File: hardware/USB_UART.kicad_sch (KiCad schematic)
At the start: 5 parts, among them U13 CP2102N-QFN20

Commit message: working on io fugtions
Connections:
- net GND: now also U13.12 (GND), U13.21 (GND), U13.3 (GND)
- no-connect marks 0 -> 4
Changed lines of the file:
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@@
   (junction (at 153.67 41.91) (diameter 0) (color 0 0 0 0)
   )
+  (no_connect (at 194.31 87.63))
+  (no_connect (at 194.31 82.55))
+  (no_connect (at 194.31 80.01))
+  (no_connect (at 194.31 85.09))
   (wire (pts (xy 165.1 62.23) (xy 168.91 62.23))
     (stroke (width 0) (type default))
@@
   )
   (wire (pts (xy 171.45 30.48) (xy 180.34 30.48))
+    (stroke (width 0) (type default))
+  )
+  (wire (pts (xy 181.61 100.33) (xy 181.61 102.87))
     (stroke (width 0) (type default))
   )
@@
         )
       )
+    )
+  )
+  (symbol (lib_name "GND_1") (lib_id "power:GND") (at 181.61 102.87 0) (unit 1)
+    (in_bom yes) (on_board yes) (dnp no) (fields_autoplaced)
+    (property "Reference" "#PWR076" (at 181.61 109.22 0)
+      (effects (font (size 1.27 1.27)) hide)
+    )
+    (property "Value" "GND" (at 181.61 107.95 0)
+      (effects (font (size 1.27 1.27)))
+    )
+    (property "Footprint" "" (at 181.61 102.87 0)
+      (effects (font (size 1.27 1.27)) hide)
+    )
+    (property "Datasheet" "" (at 181.61 102.87 0)
+      (effects (font (size 1.27 1.27)) hide)
+    )
+    (pin "1")
+    (instances
+      (project "usbc-car-module"
+        (path "/fae025e9-99c5-40c1-af6f-99dc1edbfa43/115036d9-3633-4f5d-a259-54a6f0cf58ce"
+          (reference "#PWR076") (unit 1)
+        )
+      )

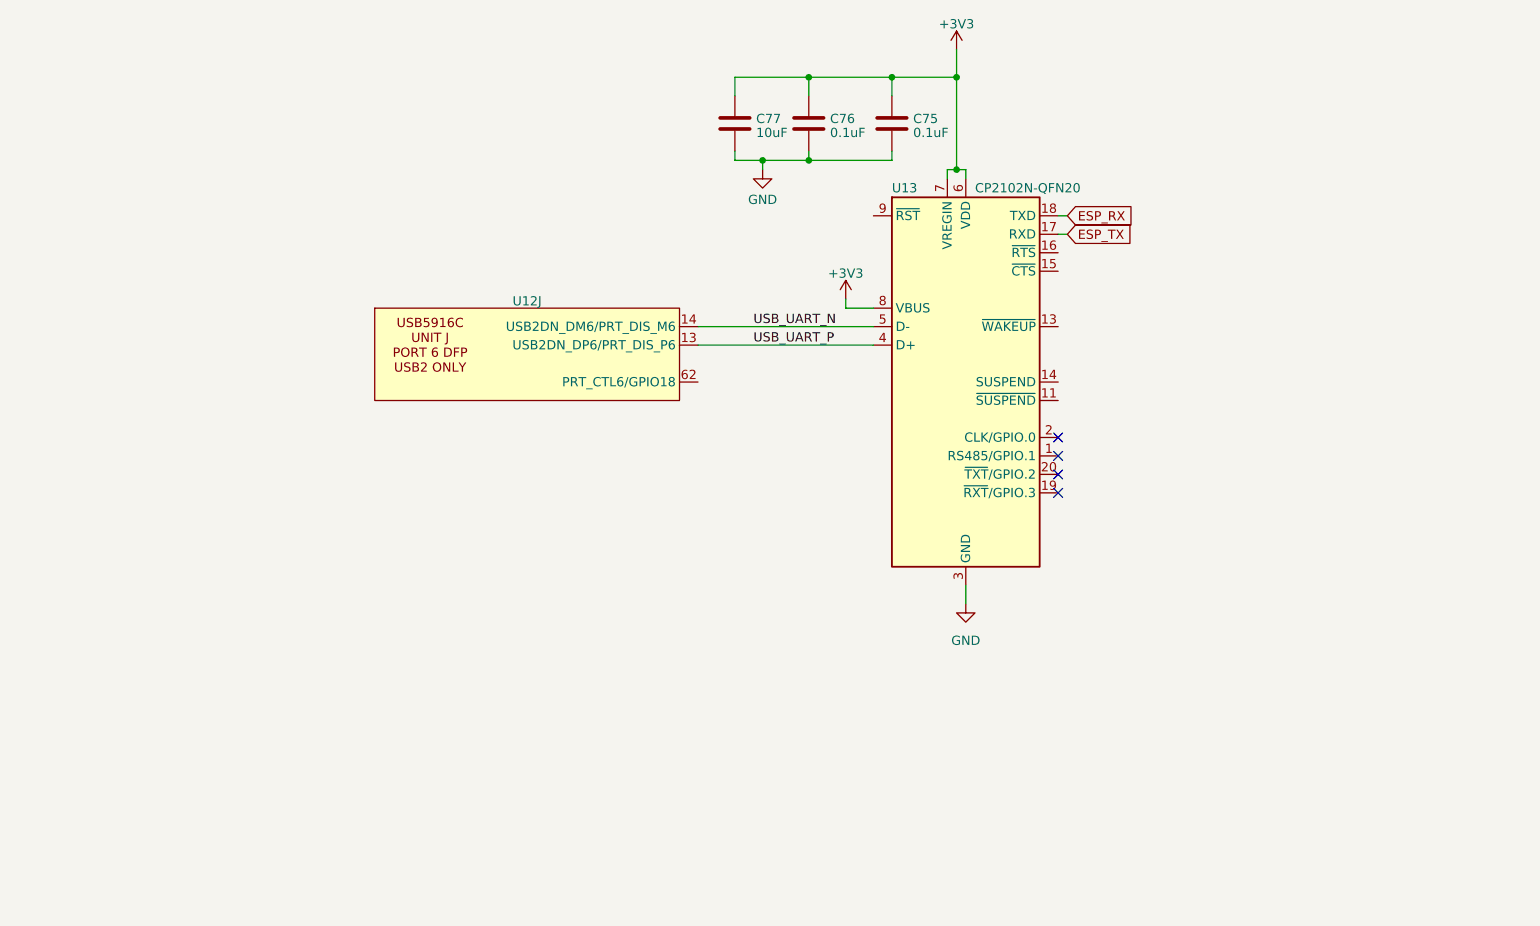
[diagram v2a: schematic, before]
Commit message: working on hardware agin as well as implimentded auto adc init and read
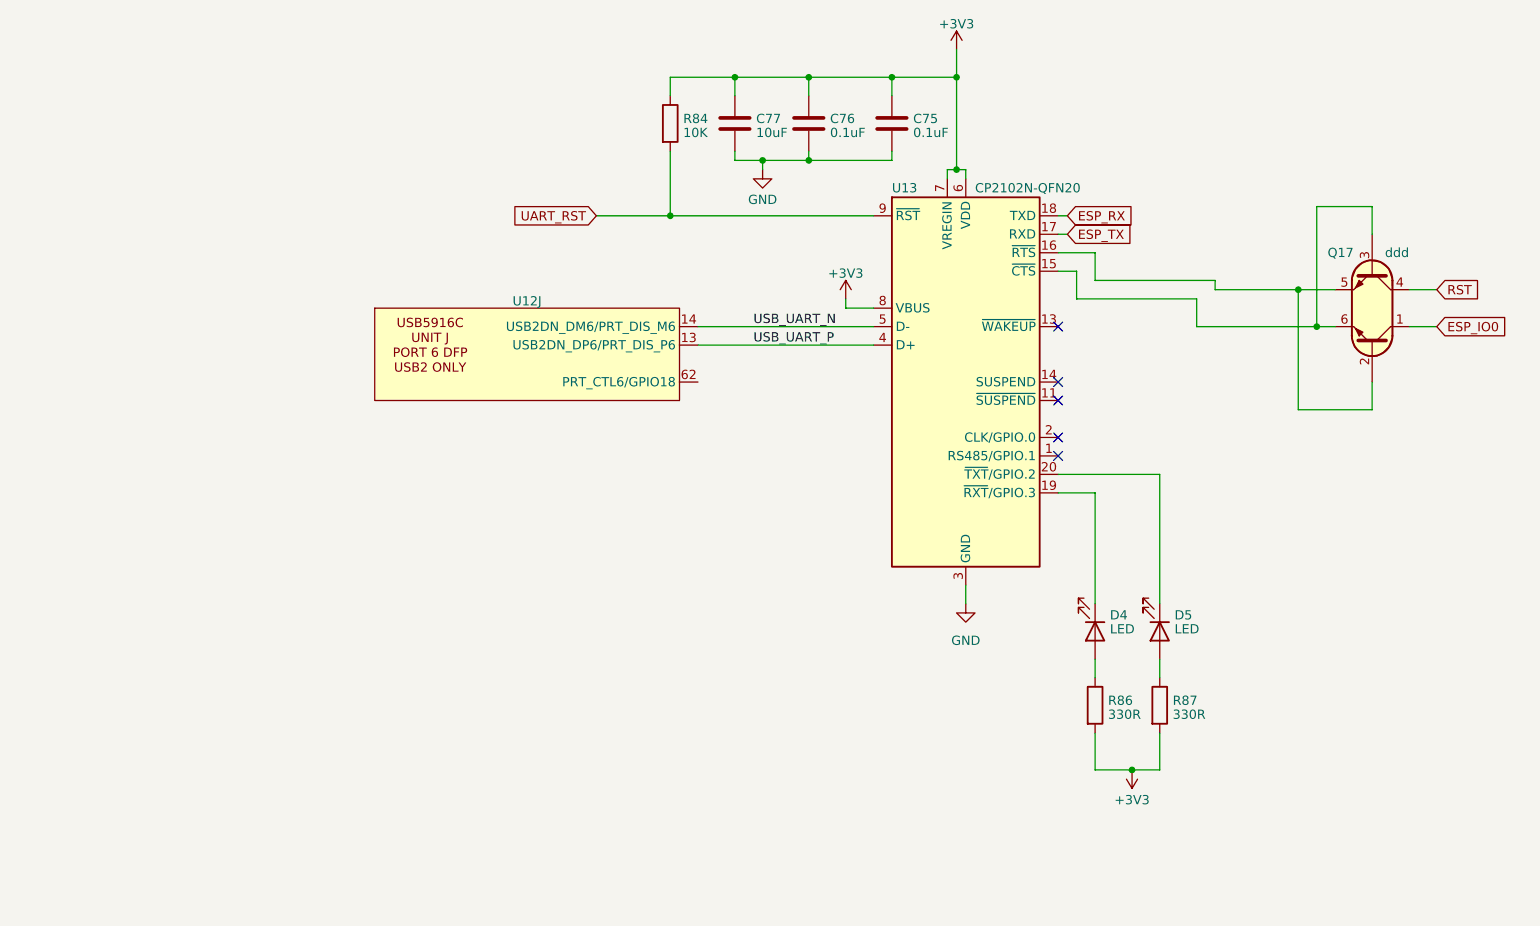
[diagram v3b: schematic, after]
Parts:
- added D4, D5: LED, symbol Device:LED
- added Q17: ddd, symbol PCM_Transistor_BJT_AKL:Q_NPN_DUAL_Generic_C1B1B2C2E2E1
- added R84: 10K, symbol Device:R
- added R86, R87: 330R, symbol Device:R
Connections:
- net +3V3: now also R84.1, R86.2, R87.2
- net at U13.15 (~{CTS}): now also Q17.3 (B2), Q17.6 (E1)
- net at U13.16 (~{RTS}): now also Q17.2 (B1), Q17.5 (E2)
- net at U13.19 (~{RXT}/GPIO.3): now also D4.1 (K)
- net at U13.20 (~{TXT}/GPIO.2): now also D5.1 (K)
- net UART_RST: now reaches U13.9 (~{RST})
- net UART_RST: now also R84.2
- new net: D5.2 (A), R87.1
- new net: D4.2 (A), R86.1
- new net ESP_IO0: Q17.1 (C1)
- new net RST: Q17.4 (C2)
- no-connect marks 4 -> 5

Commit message: working on hardware
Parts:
- added J2: ~, symbol Connector:Conn_01x01_Pin
- added TP2: ~, TestPoint:TestPoint_Pad_D1.0mm, symbol Connector:TestPoint
- added TP3: TestPoint, TestPoint:TestPoint_Pad_D1.0mm, symbol Connector:TestPoint
- C79: renamed from C77; footprint (none) -> Capacitor_SMD:C_0603_1608Metric
- C80: renamed from C76; footprint (none) -> Capacitor_SMD:C_0603_1608Metric
- C81: renamed from C75; footprint (none) -> Capacitor_SMD:C_0603_1608Metric
- D5: renamed from D4; footprint (none) -> Diode_SMD:D_0603_1608Metric
- D6: renamed from D5; footprint (none) -> Diode_SMD:D_0603_1608Metric
- renumbered R84 to R86, R86 to R87, R87 to R88, U12 to U13, U13 to U14
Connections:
- net UART_RST: now also J2.1 (Pin_1), TP2.1
- net at U13.62 (PRT_CTL6/GPIO18): now also TP3.1
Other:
- moved on the sheet: C79, C80, C81, D5, D6, Q17, R86, R87, R88, U13J, U14

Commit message: working assighning footprints still
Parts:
- R86, R87, R88: footprint (none) -> Resistor_SMD:R_0603_1608Metric
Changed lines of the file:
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@@
       (effects (font (size 1.27 1.27)) (justify left))
     )
-    (property "Footprint" "" (at 89.662 50.8 90)
+    (property "Footprint" "Resistor_SMD:R_0603_1608Metric" (at 89.662 50.8 90)
       (effects (font (size 1.27 1.27)) hide)
     )
@@
       (effects (font (size 1.27 1.27)) (justify left))
     )
-    (property "Footprint" "" (at 156.972 130.81 90)
+    (property "Footprint" "Resistor_SMD:R_0603_1608Metric" (at 156.972 130.81 90)
       (effects (font (size 1.27 1.27)) hide)
     )
@@
       (effects (font (size 1.27 1.27)) (justify left))
     )
-    (property "Footprint" "" (at 148.082 130.81 90)
+    (property "Footprint" "Resistor_SMD:R_0603_1608Metric" (at 148.082 130.81 90)
       (effects (font (size 1.27 1.27)) hide)
     )

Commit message: FINALY starting the pcb
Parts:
- J2: footprint (none) -> Connector_PinHeader_2.54mm:PinHeader_1x01_P2.54mm_Vertical
- Q17: value ddd -> BC847BS-7-F; footprint (none) -> Package_TO_SOT_SMD:SOT-363_SC-70-6
- U13: footprint (none) -> CARTHING:VQFN100_KD_MCH
- U14: footprint Package_DFN_QFN:SiliconLabs_QFN-20-1EP_3x3mm_P0.5mm -> CARTHING:QFN20_SIL
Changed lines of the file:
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@@
       (effects (font (size 1.27 1.27)) (justify right))
     )
-    (property "Value" "ddd" (at 186.69 63.5 90)
+    (property "Value" "BC847BS-7-F" (at 196.85 63.5 90)
       (effects (font (size 1.27 1.27)) (justify right))
     )
-    (property "Footprint" "" (at 196.85 71.12 0)
+    (property "Footprint" "Package_TO_SOT_SMD:SOT-363_SC-70-6" (at 196.85 71.12 0)
       (effects (font (size 1.27 1.27)) hide)
     )
@@
       (effects (font (size 1.27 1.27)))
     )
-    (property "Footprint" "" (at 63.5 55.88 0)
+    (property "Footprint" "CARTHING:VQFN100_KD_MCH" (at 63.5 55.88 0)
       (effects (font (size 1.27 1.27)) hide)
     )
@@
       (effects (font (size 1.27 1.27)) (justify left))
     )
-    (property "Footprint" "" (at 69.85 57.15 0)
+    (property "Footprint" "Connector_PinHeader_2.54mm:PinHeader_1x01_P2.54mm_Vertical" (at 69.85 57.15 0)
       (effects (font (size 1.27 1.27)) hide)
     )
@@
       (effects (font (size 1.27 1.27)) (justify left))
     )
-    (property "Footprint" "Package_DFN_QFN:SiliconLabs_QFN-20-1EP_3x3mm_P0.5mm" (at 163.83 113.03 0)
-      (effects (font (size 1.27 1.27)) hide)
-    )
+    (property "Footprint" "CARTHING:QFN20_SIL" (at 163.83 113.03 0)
+      (effects (font (size 1.27 1.27)) hide)
+    )
